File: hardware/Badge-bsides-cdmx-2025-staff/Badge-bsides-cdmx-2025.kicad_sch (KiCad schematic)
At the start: 31 parts, among them J1 SWDIO, J3 ADDON, J4 Conn_01x04_Pin, J5 I2C, J6 Conn_01x04_Pin, SW10 SW_Push, SW11 ON, SW2 RESET, SW7 SW_Push, SW8 SW_Push, SW9 SW_Push, U1 PY32F030F28U6TR

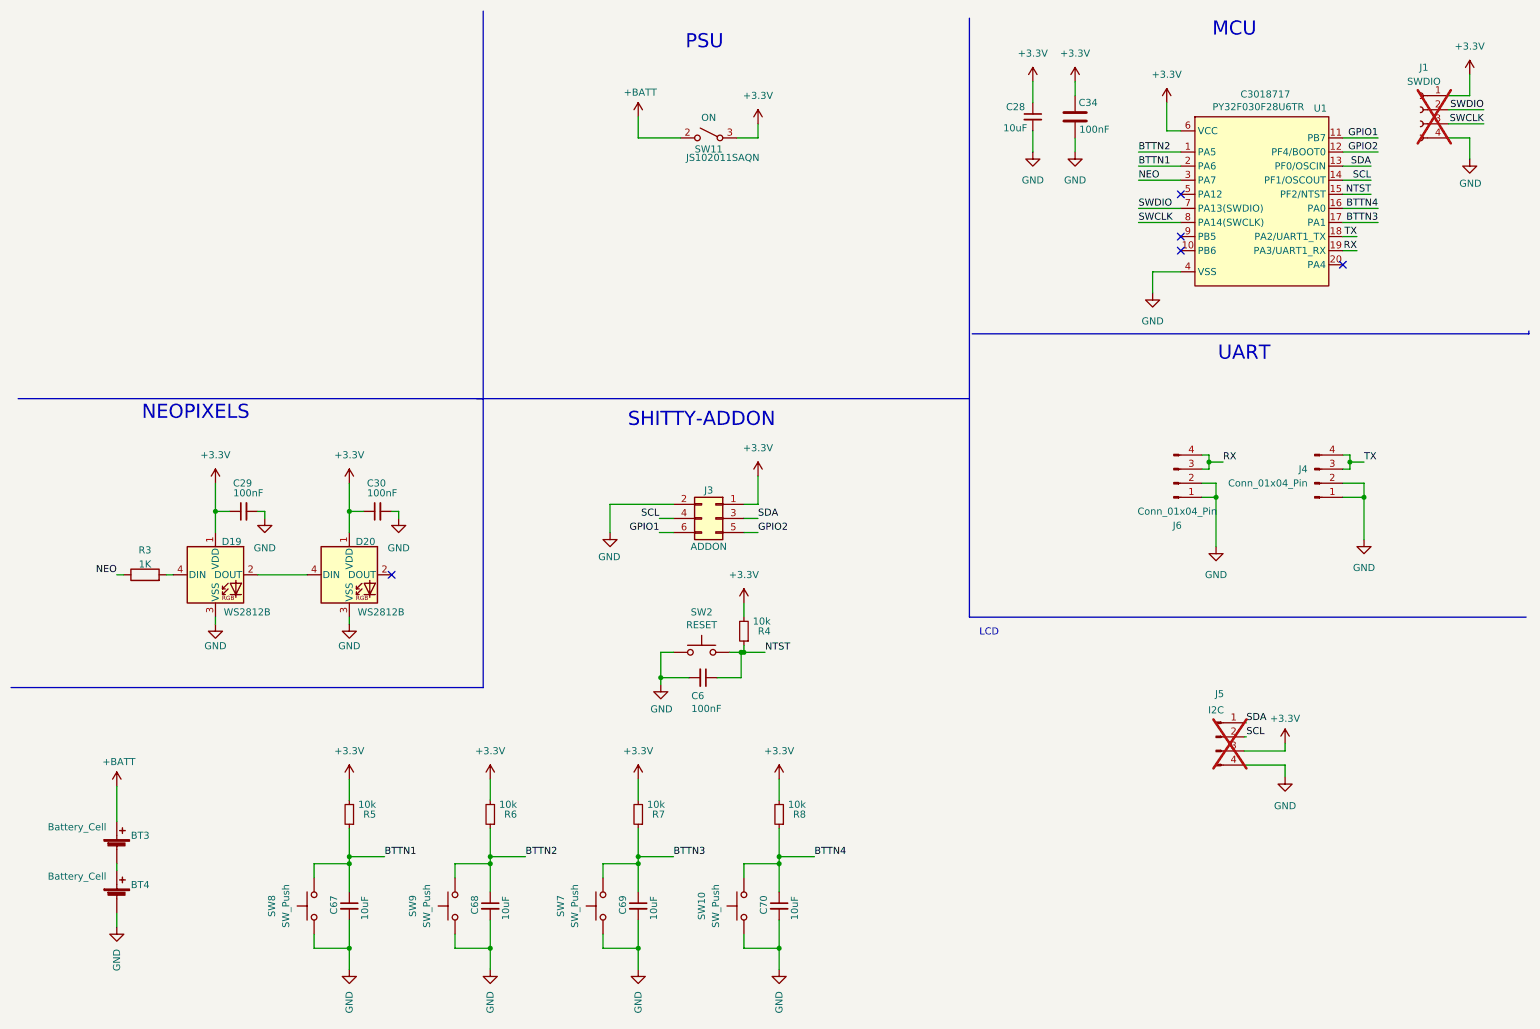
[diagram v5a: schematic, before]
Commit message: Fix(Hw): Fixed_BOM(Staff,Community, Speaker)
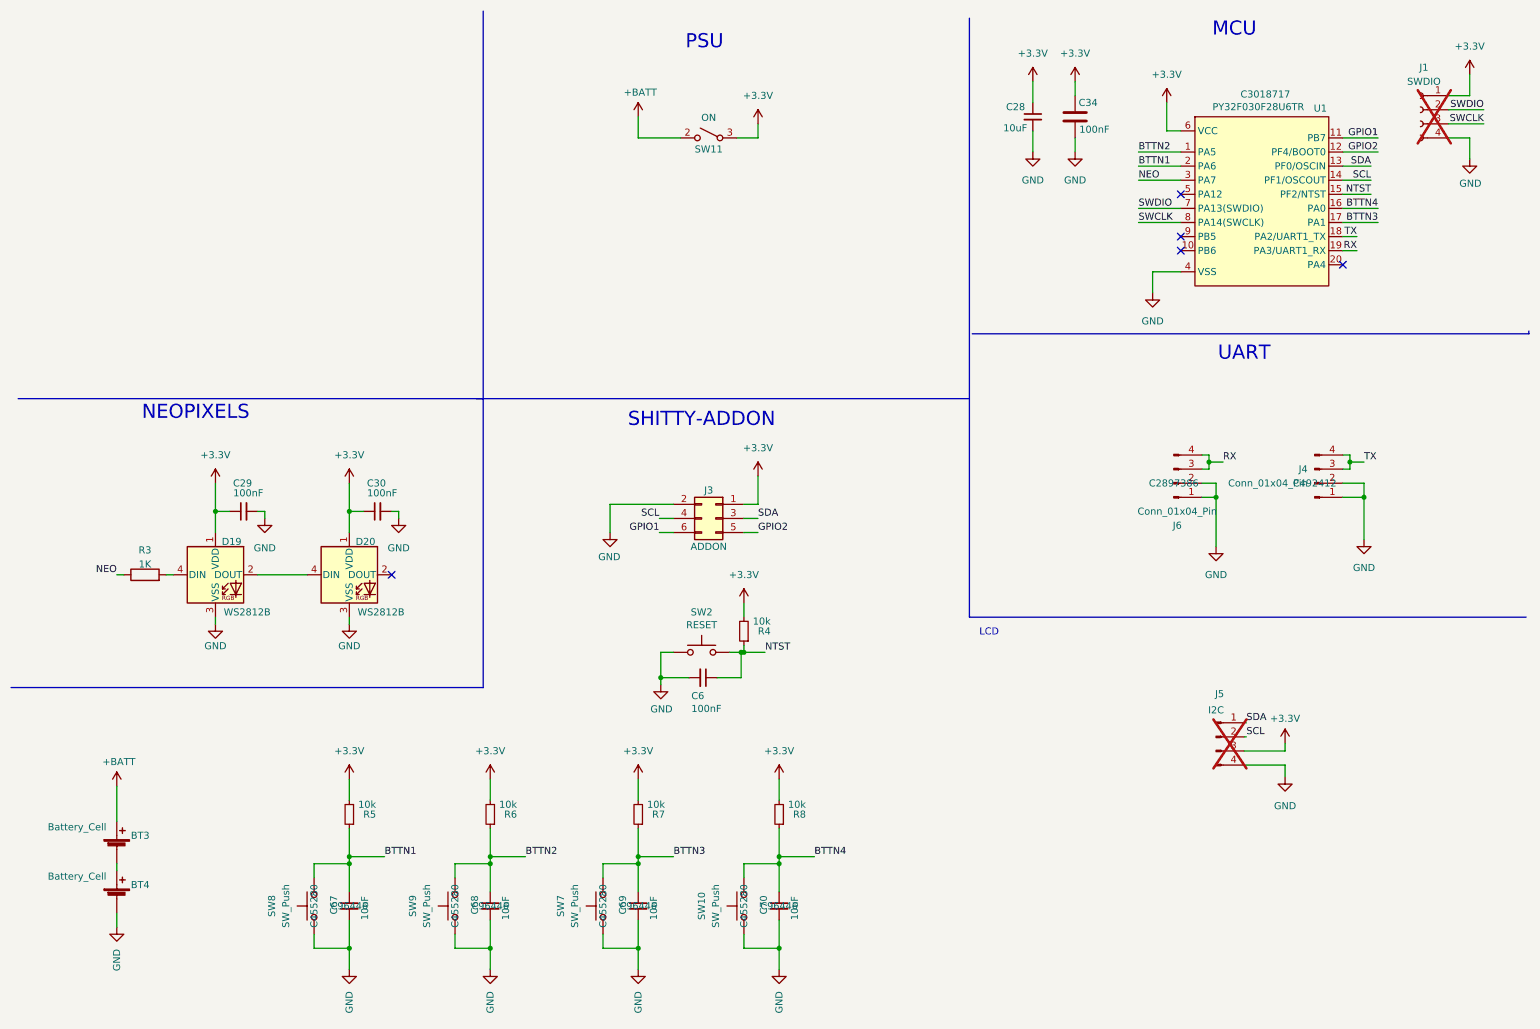
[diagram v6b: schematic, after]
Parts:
- C28: LCSC# C85713 -> C96446
- C29, C30: LCSC# C478888 -> C66501
- C34: LCSC# C14663 -> C66501
- C67, C68, C69, C70: #LCSC C96446 -> (none); LCSC# (none) -> C96446
- J4: LCSC# (none) -> C492412
- J6: LCSC# (none) -> C2897386
- SW10, SW7, SW8, SW9: #LCSC C455280 -> (none); LCSC# (none) -> C455280
- SW11: LCSC# - -> C221660; Manufacturer_Part_Number JS102011SAQN -> (none)
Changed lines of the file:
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@@
 			)
 		)
-		(property "LCSC#" "-"
+		(property "LCSC#" "C221660"
 			(at 137.16 34.29 0)
 			(effects
@@
 			)
 		)
-		(property "Manufacturer_Part_Number" "JS102011SAQN"
+		(property "Manufacturer_Part_Number" ""
 			(at 139.7 37.846 0)
 			(effects
@@
 			)
 		)
+		(property "LCSC#" "C492412"
+			(at 246.38 96.52 0)
+			(effects
+				(font
+					(size 1.27 1.27)
+				)
+			)
+		)
 		(pin "4"
 		)
@@
 			)
 		)
-		(property "LCSC#" "C85713"
+		(property "LCSC#" "C96446"
 			(at 195.58 30.48 0)
 			(effects
@@
 			)
 		)
-		(property "LCSC#" "C478888"
+		(property "LCSC#" "C66501"
 			(at 77.47 101.6 0)
 			(effects
@@
 			)
 		)
-		(property "#LCSC" "C455280"
+		(property "#LCSC" ""
 			(at 143.51 172.72 0)
 			(effects
@@
 			)
 		)
+		(property "LCSC#" "C455280"
+			(at 143.51 172.72 0)
+			(effects
+				(font
+					(size 1.27 1.27)
+				)
+			)
+		)
 		(pin "2"
 		)
@@
 			)
 		)
-		(property "#LCSC" "C96446"
+		(property "#LCSC" ""
 			(at 97.79 172.72 0)
 			(effects
@@
 			)
 		)
+		(property "LCSC#" "C96446"
+			(at 97.79 172.72 0)
+			(effects
+				(font
+					(size 1.27 1.27)
+				)
+			)
+		)
 		(pin "2"
 		)
@@
 			)
 		)
-		(property "LCSC#" "C478888"
+		(property "LCSC#" "C66501"
 			(at 53.34 101.6 0)
 			(effects
@@
 			)
 		)
+		(property "LCSC#" "C2897386"
+			(at 220.98 96.52 0)
+			(effects
+				(font
+					(size 1.27 1.27)
+				)
+			)
+		)
 		(pin "4"
 		)
@@
 			)
 		)
-		(property "#LCSC" "C96446"
+		(property "#LCSC" ""
 			(at 72.39 172.72 0)
 			(effects
@@
 			)
 		)
+		(property "LCSC#" "C96446"
+			(at 72.39 172.72 0)
+			(effects
+				(font
+					(size 1.27 1.27)
+				)
+			)
+		)
 		(pin "2"
 		)
@@
 			)
 		)
-		(property "#LCSC" "C96446"
+		(property "#LCSC" ""
 			(at 149.86 172.72 0)
 			(effects
@@
 			)
 		)
+		(property "LCSC#" "C96446"
+			(at 149.86 172.72 0)
+			(effects
+				(font
+					(size 1.27 1.27)
+				)
+			)
+		)
 		(pin "2"
 		)
@@
 			)
 		)
-		(property "#LCSC" "C455280"
+		(property "#LCSC" ""
 			(at 66.04 172.72 0)
 			(effects
@@
 			)
 		)
+		(property "LCSC#" "C455280"
+			(at 66.04 172.72 0)
+			(effects
+				(font
+					(size 1.27 1.27)
+				)
+			)
+		)
 		(pin "2"
 		)
@@
 			)
 		)
-		(property "LCSC#" "C14663"
+		(property "LCSC#" "C66501"
 			(at 209.296 30.48 0)
 			(effects
@@
 			)
 		)
-		(property "#LCSC" "C455280"
+		(property "#LCSC" ""
 			(at 118.11 172.72 0)
 			(effects
@@
 			)
 		)
+		(property "LCSC#" "C455280"
+			(at 118.11 172.72 0)
+			(effects
+				(font
+					(size 1.27 1.27)
+				)
+			)
+		)
 		(pin "2"
 		)
@@
 			)
 		)
-		(property "#LCSC" "C96446"
+		(property "#LCSC" ""
 			(at 124.46 172.72 0)
 			(effects
@@
 			)
 		)
+		(property "LCSC#" "C96446"
+			(at 124.46 172.72 0)
+			(effects
+				(font
+					(size 1.27 1.27)
+				)
+			)
+		)
 		(pin "2"
 		)
@@
 			)
 		)
-		(property "#LCSC" "C455280"
+		(property "#LCSC" ""
 			(at 91.44 172.72 0)
 			(effects
@@
 			(at 91.44 172.72 0)
 			(effects
+				(font
+					(size 1.27 1.27)
+				)
+			)
+		)
+		(property "LCSC#" "C455280"
+			(at 91.44 172.72 0)
+			(effects

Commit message: fix(Hw):Labels_Updated
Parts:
- R3: value 1K -> 470R; LCSC# C22548 -> C114669
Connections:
- net GND: now also U1.21 (VSS)
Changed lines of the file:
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@@
 			)
 		)
-		(property "Value" "1K"
+		(property "Value" "470R"
 			(at 35.56 111.125 90)
 			(effects
@@
 			)
 		)
-		(property "LCSC#" "C22548"
+		(property "LCSC#" "C114669 "
 			(at 35.56 113.03 0)
 			(effects
@@
 		(pin "12"
 		)
+		(pin "21"
+		)
 		(instances
